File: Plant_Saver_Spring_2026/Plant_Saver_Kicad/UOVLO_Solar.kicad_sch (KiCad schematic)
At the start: 11 parts, among them Q11 ISP12DP06NMXTSA1, Q12 G09P02L, U16 MCP6547T_I_MS

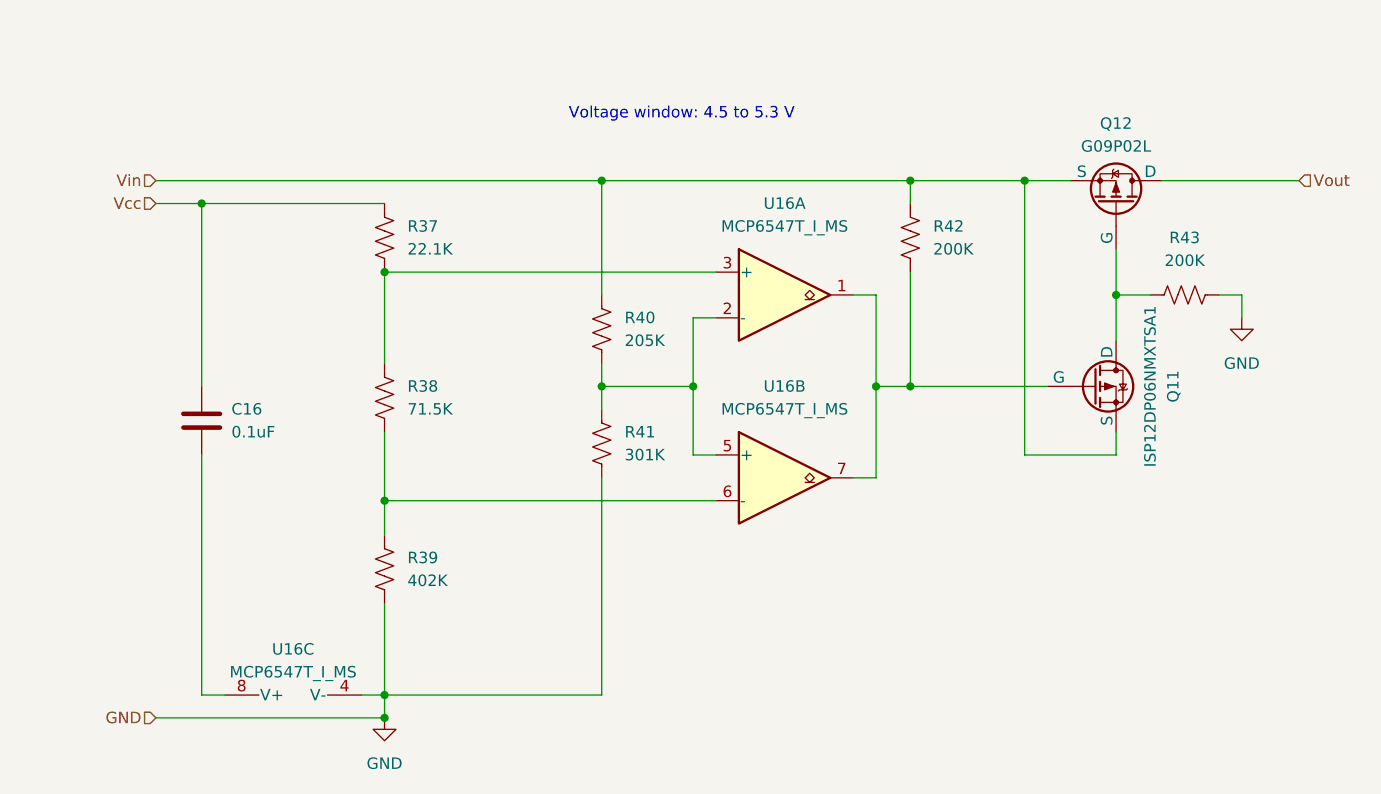
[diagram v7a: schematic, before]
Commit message: Re-routed to fix issue on schematic
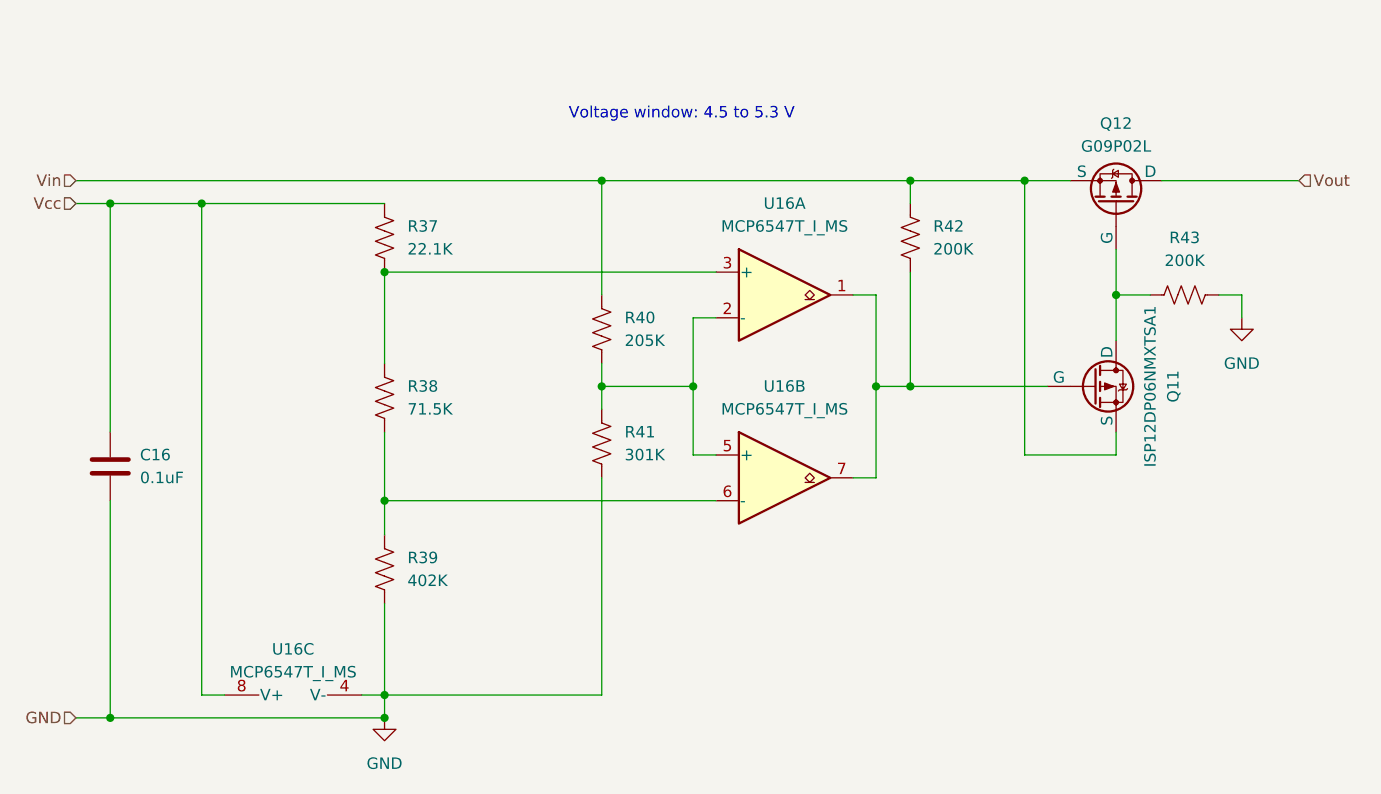
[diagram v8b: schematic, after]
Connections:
- net GND: now also C16.2
- net Vcc: now also U16.8 (V+)
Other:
- moved on the sheet: C16
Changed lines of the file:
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@@
+	)
+	(junction
+		(at 83.82 71.12)
+		(diameter 0)
+		(color 0 0 0 0)
 	)
 	(junction
@@
 	)
 	(junction
+		(at 83.82 128.27)
+		(diameter 0)
+		(color 0 0 0 0)
+	)
+	(junction
 		(at 114.3 125.73)
 		(diameter 0)
@@
 	(wire
 		(pts
+			(xy 83.82 71.12) (xy 93.98 71.12)
+		)
+		(stroke
+			(width 0)
+			(type default)
+		)
+	)
+	(wire
+		(pts
 			(xy 96.52 125.73) (xy 93.98 125.73)
 		)
@@
 	(wire
 		(pts
-			(xy 88.9 128.27) (xy 114.3 128.27)
+			(xy 80.01 128.27) (xy 83.82 128.27)
 		)
 		(stroke
@@
 	(wire
 		(pts
-			(xy 93.98 71.12) (xy 93.98 91.44)
-		)
-		(stroke
-			(width 0)
-			(type default)
-		)
-	)
-	(wire
-		(pts
 			(xy 114.3 115.57) (xy 114.3 125.73)
 		)
@@
 	(wire
 		(pts
-			(xy 93.98 99.06) (xy 93.98 125.73)
+			(xy 93.98 71.12) (xy 93.98 125.73)
 		)
 		(stroke
@@
 	(wire
 		(pts
-			(xy 88.9 71.12) (xy 93.98 71.12)
-		)
-		(stroke
-			(width 0)
-			(type default)
-		)
-	)
-	(wire
-		(pts
-			(xy 88.9 68.58) (xy 138.43 68.58)
+			(xy 80.01 71.12) (xy 83.82 71.12)
+		)
+		(stroke
+			(width 0)
+			(type default)
+		)
+	)
+	(wire
+		(pts
+			(xy 80.01 68.58) (xy 138.43 68.58)
 		)
 		(stroke
@@
 	(wire
 		(pts
+			(xy 83.82 104.14) (xy 83.82 128.27)
+		)
+		(stroke
+			(width 0)
+			(type default)
+		)
+	)
+	(wire
+		(pts
 			(xy 195.58 86.36) (xy 195.58 81.28)
 		)
@@
 		(pts
 			(xy 185.42 68.58) (xy 190.5 68.58)
+		)
+		(stroke
+			(width 0)
+			(type default)
+		)
+	)
+	(wire
+		(pts
+			(xy 83.82 128.27) (xy 114.3 128.27)
+		)
+		(stroke
+			(width 0)
+			(type default)
+		)
+	)
+	(wire
+		(pts
+			(xy 83.82 71.12) (xy 83.82 96.52)
 		)
 		(stroke
@@
 	(hierarchical_label "Vin"
 		(shape input)
-		(at 88.9 68.58 180)
+		(at 80.01 68.58 180)
 		(effects
 			(font
@@
 	(hierarchical_label "GND"
 		(shape input)
-		(at 88.9 128.27 180)
+		(at 80.01 128.27 180)
 		(effects
 			(font
@@
 	(hierarchical_label "Vcc"
 		(shape input)
-		(at 88.9 71.12 180)
+		(at 80.01 71.12 180)
 		(effects
 			(font
@@
 	(symbol
 		(lib_id "Device:C")
-		(at 93.98 95.25 0)
+		(at 83.82 100.33 0)
 		(unit 1)
 		(exclude_from_sim no)
@@
 		(dnp no)
 		(property "Reference" "C16"
-			(at 97.282 93.98 0)
+			(at 87.122 99.06 0)
 			(effects
 				(font
@@
 		)
 		(property "Value" "0.1uF"
-			(at 97.282 96.52 0)
+			(at 87.122 101.6 0)
 			(effects
 				(font
@@
 		)
 		(property "Footprint" "Capacitor_SMD:C_1206_3216Metric_Pad1.33x1.80mm_HandSolder"
-			(at 94.9452 99.06 0)
+			(at 84.7852 104.14 0)
 			(effects
 				(font
@@
 		)
 		(property "Datasheet" "~"
-			(at 93.98 95.25 0)
+			(at 83.82 100.33 0)
 			(effects
 				(font
@@
 		)
 		(property "Description" "Unpolarized capacitor"
-			(at 93.98 95.25 0)
+			(at 83.82 100.33 0)
 			(effects
 				(font
@@
 		)
 		(property "Field5" "CL31A106KBHNNNE"
-			(at 93.98 95.25 0)
-			(effects
-				(font
+			(at 83.82 100.33 0)
+			(effects
+				(font
